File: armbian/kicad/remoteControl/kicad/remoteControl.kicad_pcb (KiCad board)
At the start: 2 copper layers, 162.6 x 101.6 mm, 29 parts, among them J1 Conn_01x02, J2 USB_2, P1 CONN_1, P10 CONN_2, P11 CONN_1, P12 CONN_1, P13 CONN_1, P14 CONN_15, P15 CONN_1, P16 CONN_1, P17 CONN_1, P2 CONN_1, P3 PI, P4 CONN_5, P5 CONN_4X1, P6 CONN_3, P7 CONN_4X1, P8 CONN_2, P9 CONN_2, U1 BUCK

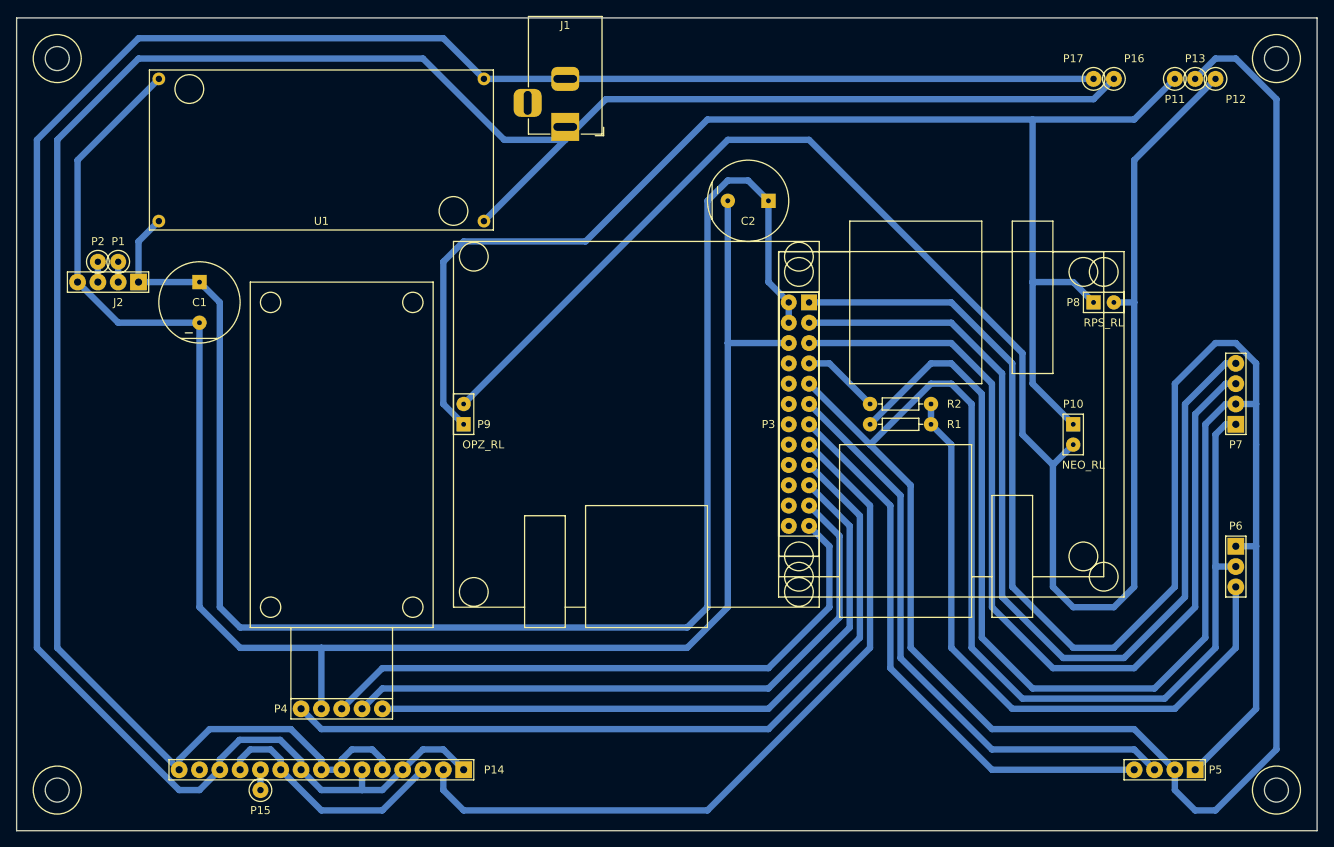
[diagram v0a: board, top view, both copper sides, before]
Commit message: armbian: wip (not tested): remoteControl pcb (2)
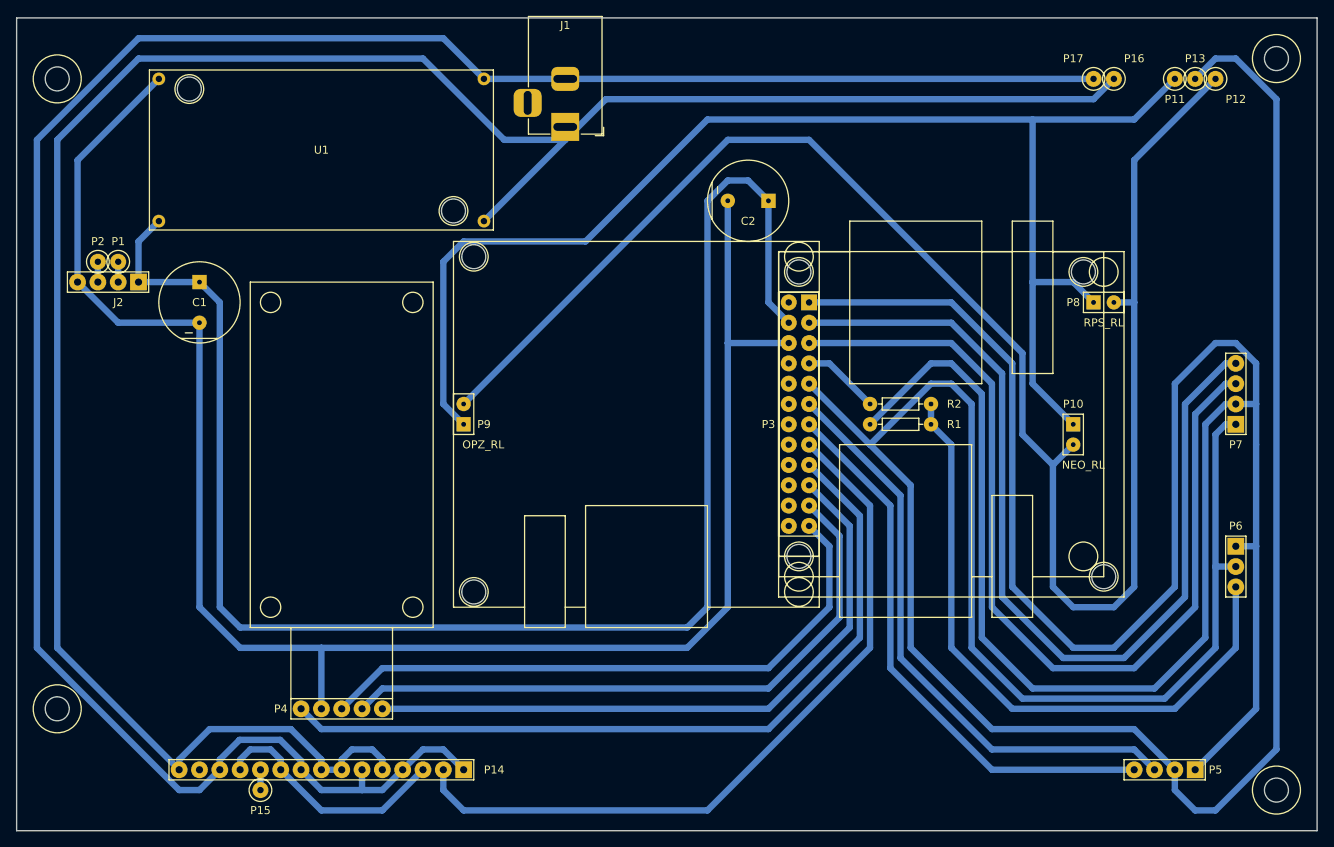
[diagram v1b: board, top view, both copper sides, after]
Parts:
- moved REF** 10.2 mm to (45.7, 111.8)
- moved REF** 2.54 mm to (45.7, 33.0)
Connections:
- P3 pad 2: Net-(C1-Pad1) -> (no net)

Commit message: armbian: wip (not tested): remoteControl pcb (3)
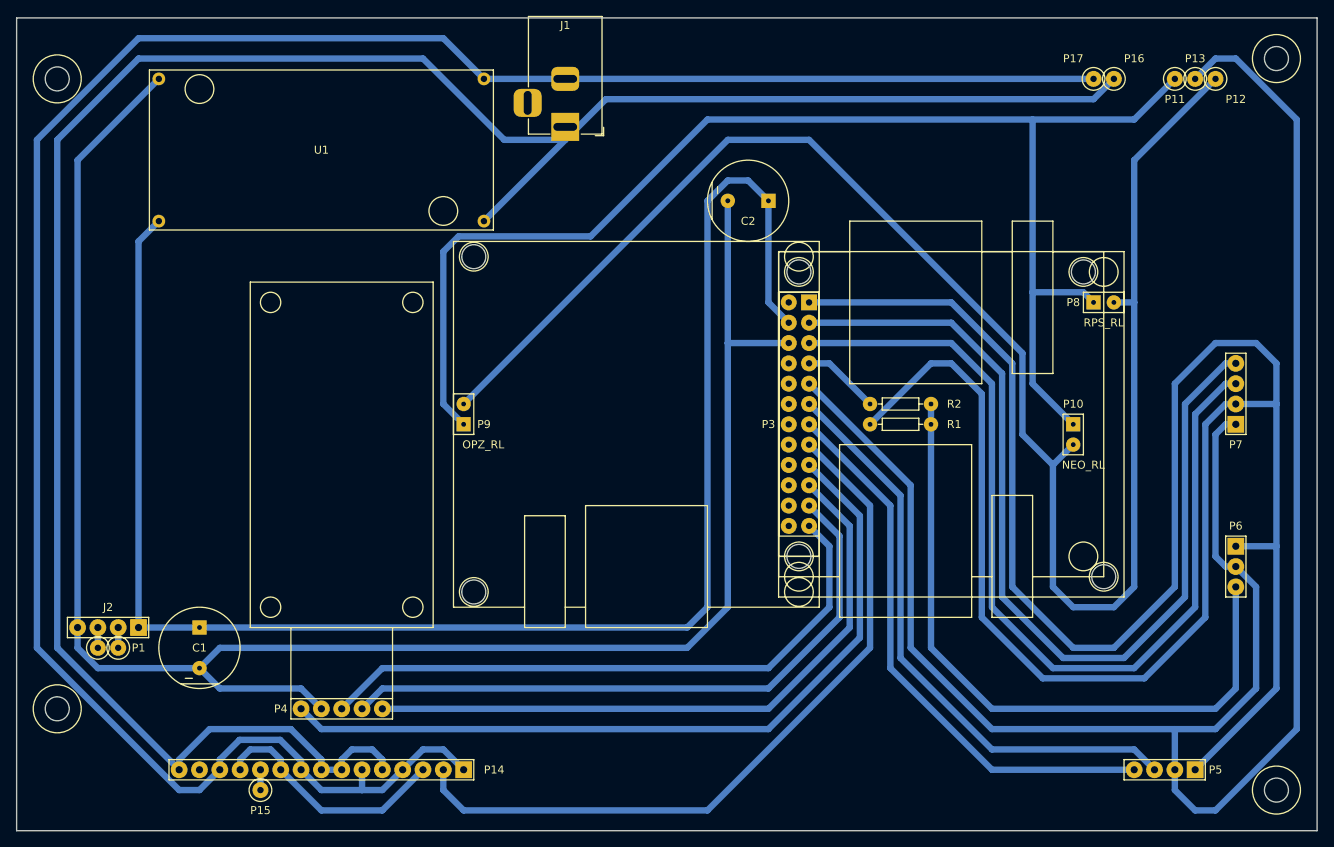
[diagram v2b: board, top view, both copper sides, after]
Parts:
- moved P1 48.3 mm to (53.3, 104.1)
- moved P2 48.3 mm to (50.8, 104.1)
- moved C1 43.2 mm to (63.5, 104.1)
- moved J2 43.2 mm to (52.1, 101.6)
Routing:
- net Net-(P13-Pad1): track 307.1 -> 246.7 mm
- net Net-(C1-Pad2): track 218.8 -> 236.6 mm
- net Net-(P3-Pad1): track 294.8 -> 299.4 mm
- net Net-(P6-Pad3): track 81.0 -> 85.5 mm
- net Net-(C1-Pad1): track 197.9 -> 200.8 mm

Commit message: armbian: wip (rc not tested): remoteControl pcb (4)
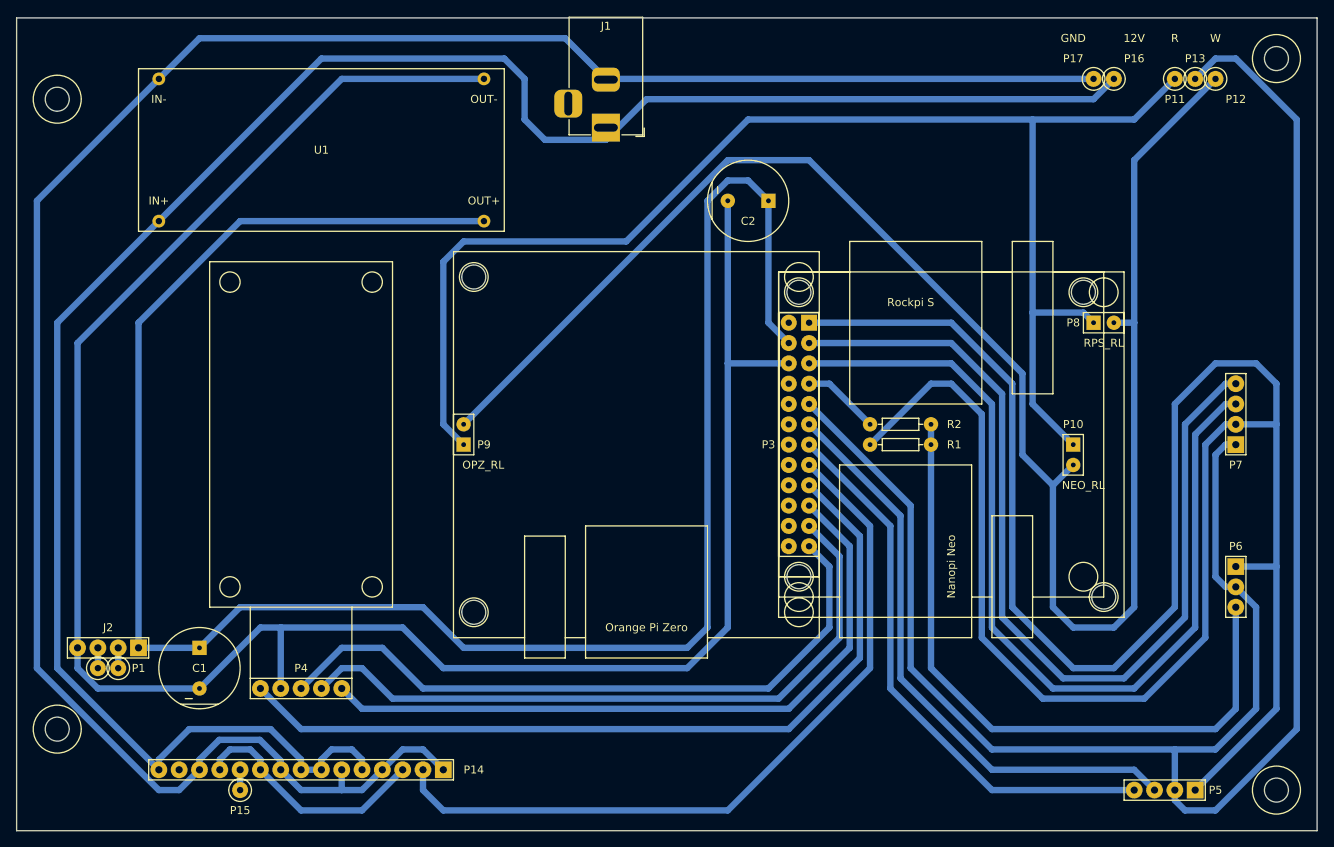
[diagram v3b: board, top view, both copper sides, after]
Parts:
- U1: value BUCK -> BUCK_MAKERFACTORY; footprint kicad:BUCK -> kicad:BUCK_MAKERFACTORY
- moved P4 5.68 mm to (76.2, 109.2)
- moved J1 5.08 mm to (114.3, 39.1)
- moved C1 2.54 mm to (63.5, 106.7)
- moved J2 2.54 mm to (52.1, 104.1)
- moved P1 2.54 mm to (53.3, 106.7)
- moved P10 2.54 mm to (172.7, 80.0)
- moved P15 2.54 mm to (68.6, 121.9)
- moved P2 2.54 mm to (50.8, 106.7)
- moved P5 2.54 mm to (184.2, 121.9)
- moved P7 2.54 mm to (193.0, 74.9)
- moved R2 2.54 mm to (152.4, 76.2)
- moved P8 2.54 mm to (176.5, 63.5)
- moved REF** 2.54 mm to (45.7, 35.6)
- moved P14 2.54 mm to (76.2, 119.4)
- moved P3 2.54 mm to (139.7, 78.7)
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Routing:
- net Net-(C1-Pad1): track 200.8 -> 247.4 mm
- net Net-(C1-Pad2): track 236.6 -> 263.4 mm
- net Net-(J1-Pad1): track 279.4 -> 253.5 mm
- net Net-(P3-Pad23): track 77.4 -> 84.6 mm
- net Net-(P3-Pad21): track 80.0 -> 86.1 mm
- net Net-(J1-Pad2): track 275.9 -> 270.4 mm
- net Net-(P3-Pad19): track 82.5 -> 87.6 mm
- net Net-(P3-Pad17): track 99.9 -> 104.9 mm
- net Net-(P10-Pad1): track 171.4 -> 175.7 mm
- net Net-(P10-Pad2): track 211.5 -> 214.0 mm
- net Net-(P13-Pad1): track 246.7 -> 244.9 mm
- net Net-(P14-Pad2): track 93.9 -> 95.4 mm
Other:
- board text added: "12V"
- board text added: "GND"
- board text added: "R"
- board text added: "W"

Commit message: armbian/kicad/remoteControl: change rc module (not tested)
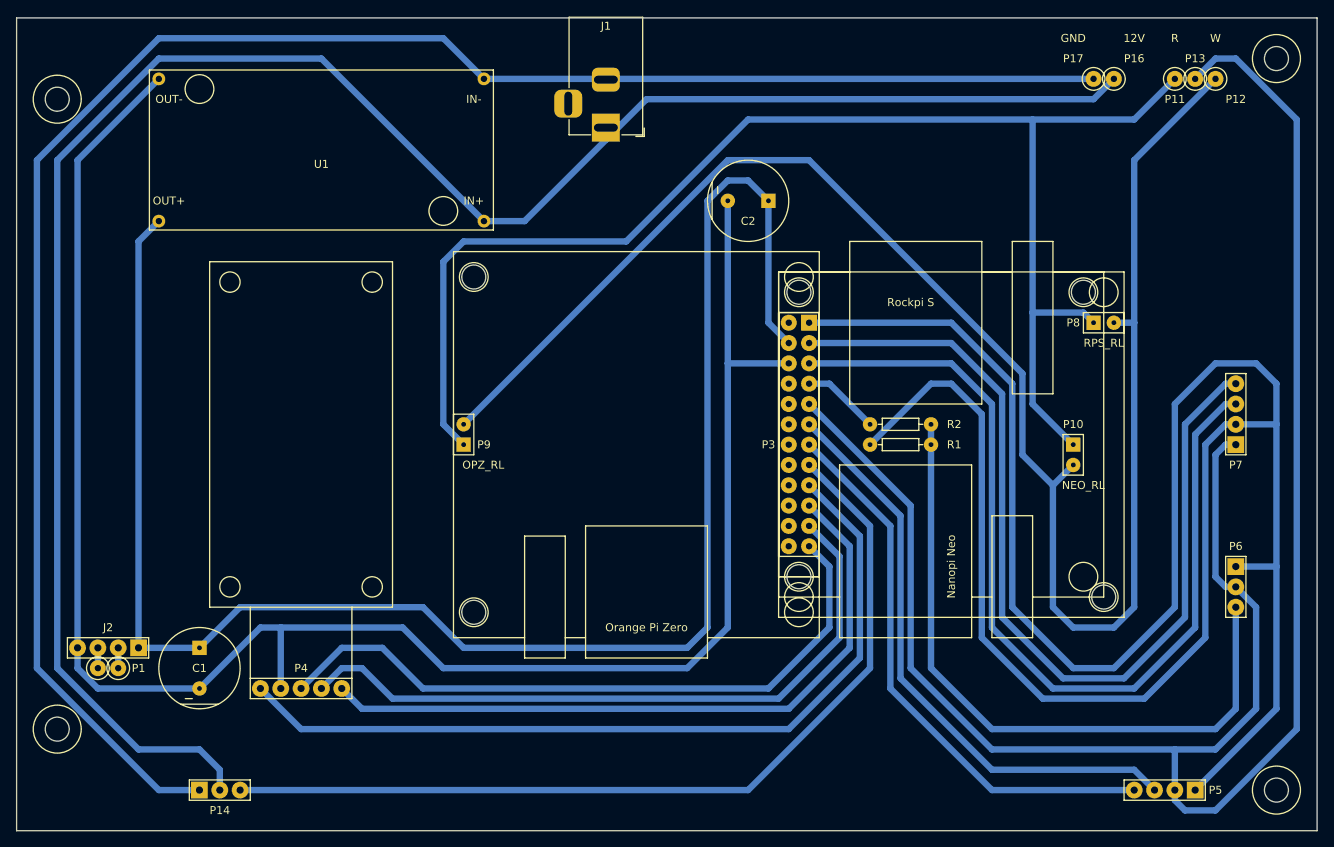
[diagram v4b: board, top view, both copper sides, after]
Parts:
- removed P15: CONN_1, kicad:PIN_ARRAY_1X1
- P14: value CONN_15 -> CONN_3; footprint kicad:PIN_ARRAY_15X1 -> kicad:PIN_ARRAY_3X1
- U1: value BUCK_MAKERFACTORY -> BUCK; footprint kicad:BUCK_MAKERFACTORY -> kicad:BUCK
- moved P14 10.5 mm to (66.0, 121.9), turned to 0 degrees
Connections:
- P14 pad 2: Net-(P14-Pad2) -> Net-(J1-Pad1)
- P14 pad 3: Net-(P14-Pad10) -> Net-(P14-Pad3)
- P3 pad 15: Net-(P14-Pad2) -> Net-(P14-Pad3)
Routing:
- net Net-(P14-Pad3): track 0.00 -> 113.6 mm
- net Net-(P14-Pad2): track 95.4 -> 0.00 mm
- net Net-(J1-Pad2): track 270.4 -> 230.7 mm
- net Net-(C1-Pad1): track 247.4 -> 212.7 mm
- net Net-(P14-Pad10): track 30.7 -> 0.00 mm
- net Net-(C1-Pad2): track 263.4 -> 236.1 mm
- net Net-(J1-Pad1): track 253.5 -> 246.3 mm
- net Net-(P14-Pad11): track 2.54 -> 0.00 mm

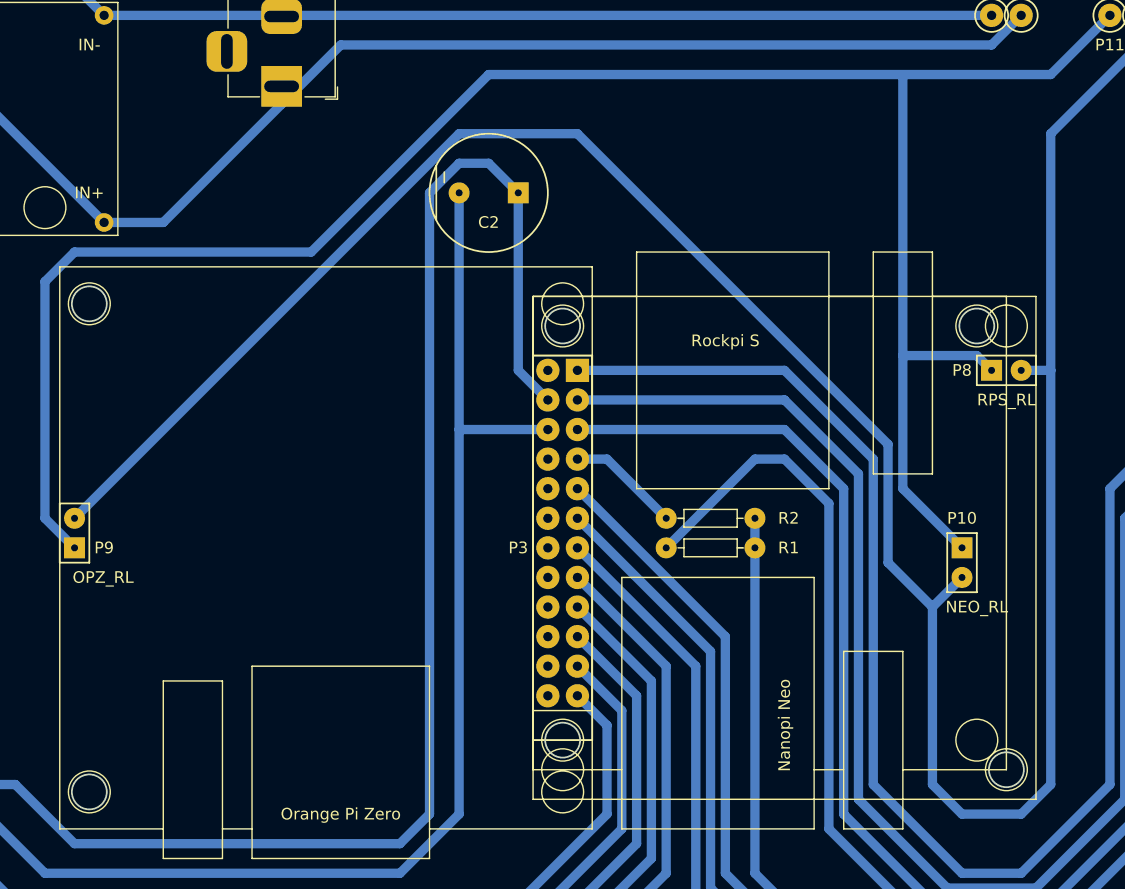
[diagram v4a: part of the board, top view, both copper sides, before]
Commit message: armbian/kicad/remoteControl: shift capacitor
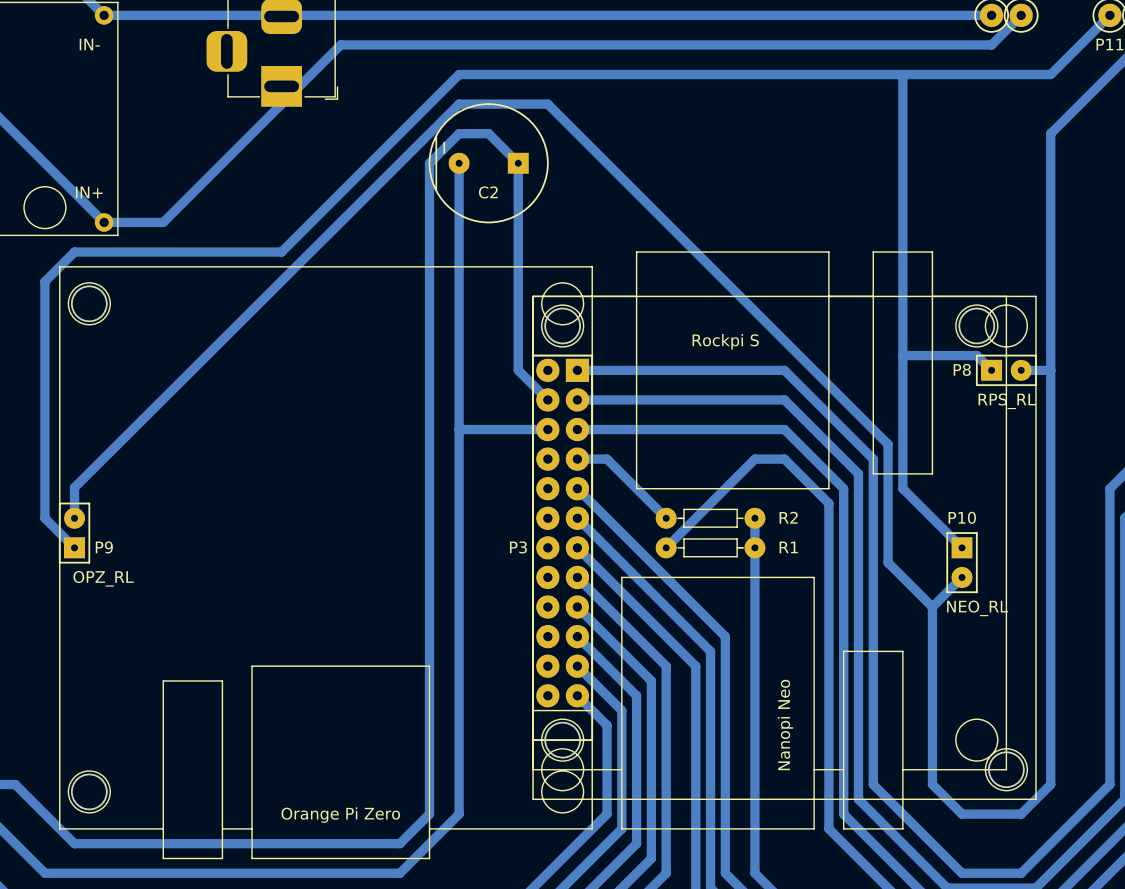
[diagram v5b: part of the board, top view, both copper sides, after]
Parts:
- moved C2 2.54 mm to (132.1, 45.7)
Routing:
- net Net-(C1-Pad1): track 212.7 -> 217.7 mm
- net Net-(P10-Pad2): track 214.0 -> 217.6 mm
- net Net-(C1-Pad2): track 236.1 -> 238.7 mm

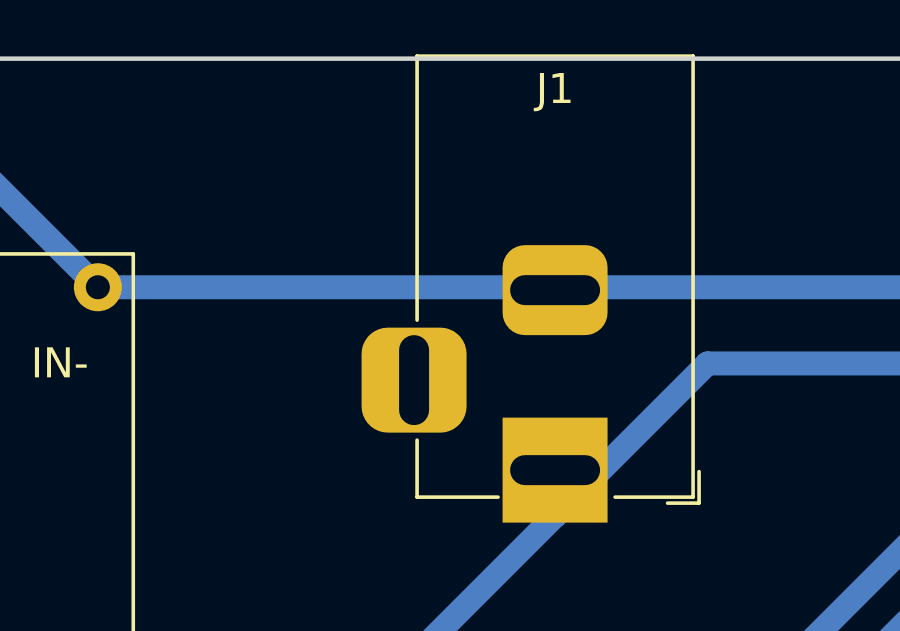
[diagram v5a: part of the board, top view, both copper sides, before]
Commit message: armbian/kicad/remoteControl: two drills have a diameter of 2.5mm
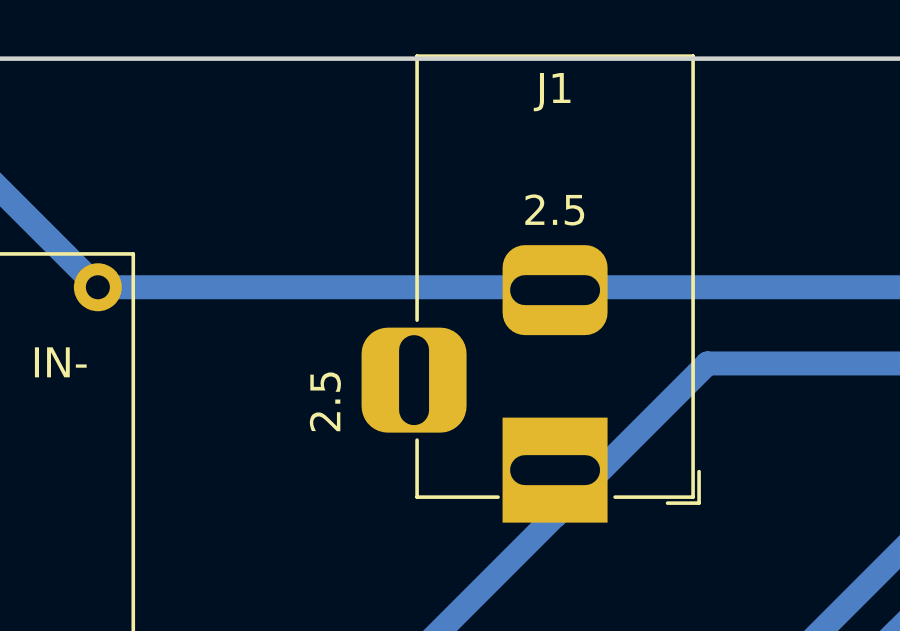
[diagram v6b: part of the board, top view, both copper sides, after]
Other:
- board text added: "2.5"
